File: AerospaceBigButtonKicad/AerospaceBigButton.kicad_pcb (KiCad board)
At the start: 2 copper layers, 120 x 80 mm, 20 parts, among them J1 Conn_01x07, J2 Conn_01x07, J3 Conn_01x02, J4 Conn_01x02, J5 Conn_01x02, Q1 Si7336ADP, SW1 BIGSWITCH, U1 AMS1117-5.0

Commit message: basic design done
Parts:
- removed R6: 100k, Resistor_SMD:R_0805_2012Metric
- removed R7: 27k, Resistor_SMD:R_0805_2012Metric
- added H1: MountingHole_Pad, MountingHole:MountingHole_3.2mm_M3_DIN965_Pad_TopBottom, F.Cu at (55.0, 20.0)
- added H2: MountingHole_Pad, MountingHole:MountingHole_3.2mm_M3_DIN965_Pad_TopBottom, F.Cu at (160.0, 20.0)
- added H3: MountingHole_Pad, MountingHole:MountingHole_3.2mm_M3_DIN965_Pad_TopBottom, F.Cu at (160.0, 90.0)
- added H4: MountingHole_Pad, MountingHole:MountingHole_3.2mm_M3_DIN965_Pad_TopBottom, F.Cu at (55.0, 90.0)
- added J6: Conn_01x03, Connector_JST:JST_PH_B3B-PH-K_1x03_P2.00mm_Vertical, F.Cu at (54.9, 56.4)
- moved R1 92.6 mm to (86.0, 77.7), turned to 90 degrees
- moved C1 89.0 mm to (81.2, 33.0)
- moved R4 86.3 mm to (85.8, 71.0)
- moved R5 85.0 mm to (85.8, 73.6), turned to 180 degrees
- moved R2 78.7 mm to (76.6, 57.6)
- moved R3 78.7 mm to (76.6, 59.8)
- moved R8 78.6 mm to (85.3, 58.2), turned to -90 degrees
- moved R9 75.1 mm to (81.8, 58.2), turned to -90 degrees
- moved C2 74.1 mm to (67.4, 54.8)
- moved U1 5.55 mm to (65.8, 48.6)
- moved J2 2.54 mm to (81.3, 63.5)
- moved SW1 2.46 mm to (125.0, 55.0)
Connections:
- J2 pad 3: /RGB -> /CONT
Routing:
- net Net-(Q1-G): track 0.00 -> 71.8 mm
- net +3V3: track 0.00 -> 52.5 mm
- net /BIGSWITCH: track 0.00 -> 50.5 mm
- net Net-(J4-Pin_1): track 0.00 -> 37.8 mm, vias 0 -> 2
- net /ARMED: track 0.00 -> 30.4 mm
- net VCC: track 0.00 -> 26.7 mm
- net +5V: track 0.00 -> 22.4 mm
- net /CONT: track 0.00 -> 13.1 mm
- net /VINSENSE: track 0.00 -> 9.63 mm
- net /FIRE: track 0.00 -> 6.23 mm
- net GND: vias 0 -> 32
- added copper zone on F.Cu, net /PYRO
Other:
- board size 120 x 80 mm -> 114.2 x 80.2 mm

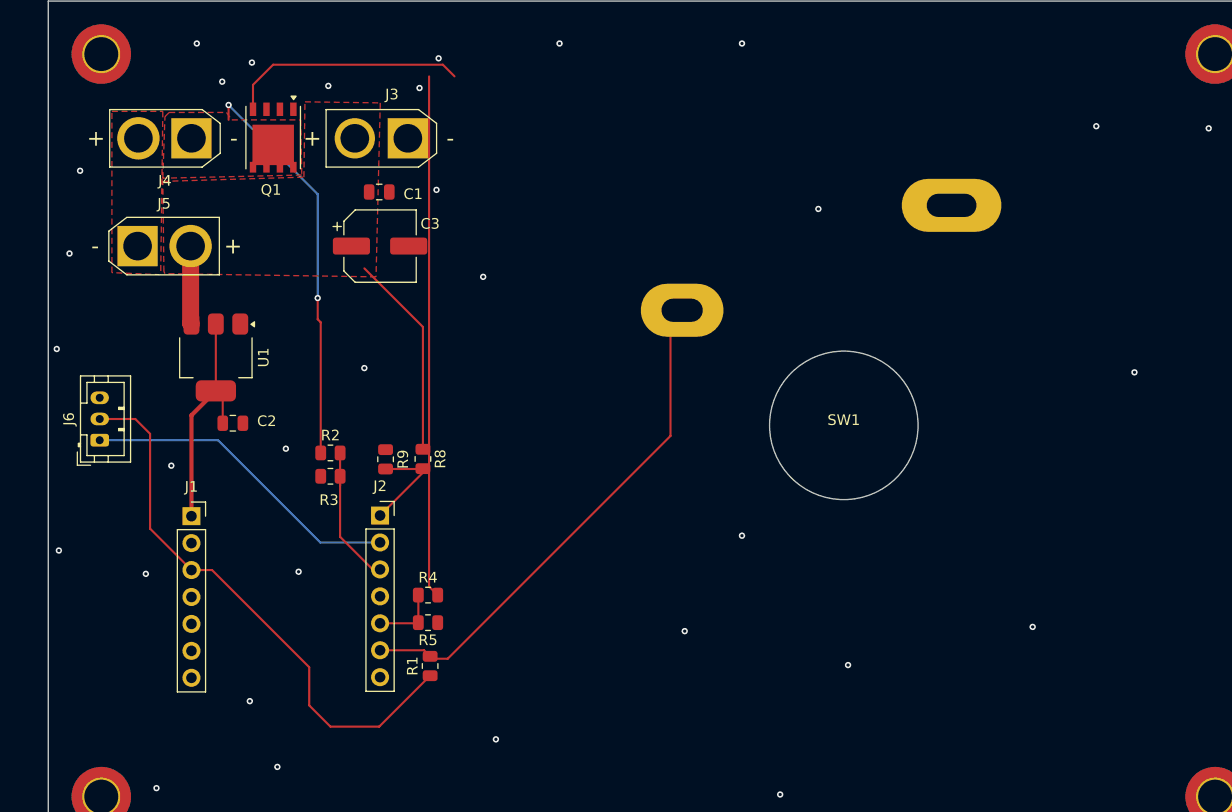
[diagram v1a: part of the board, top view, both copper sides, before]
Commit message: finalized design for now, added 5v driver for speaker
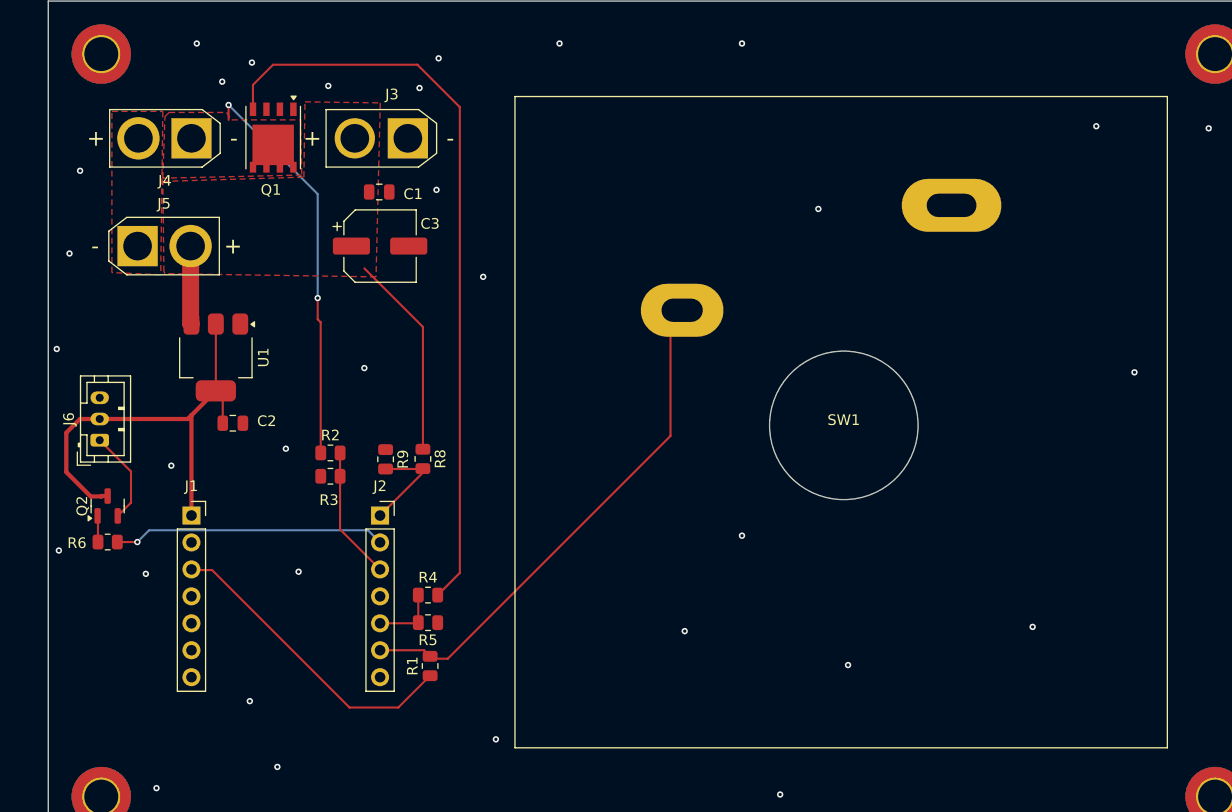
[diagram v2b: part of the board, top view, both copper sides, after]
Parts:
- added Q2: MMBT2222A, Package_TO_SOT_SMD:SOT-23, F.Cu at (55.6, 62.6)
- added R6: 1k, Resistor_SMD:R_0805_2012Metric, F.Cu at (55.6, 66.0)
- moved J1 0.06 mm to (63.5, 63.5)
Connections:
- J6 pad 1: /ARMED -> Net-(J6-Pin_1)
- J6 pad 2: +3V3 -> +5V
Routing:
- net +3V3: track 52.5 -> 29.1 mm
- net +5V: track 22.4 -> 43.4 mm
- net Net-(J6-Pin_1): track 0.00 -> 8.88 mm
- net /ARMED: track 30.4 -> 25.7 mm, vias 0 -> 1
- net Net-(Q2-B): track 0.00 -> 2.48 mm
- net Net-(Q1-G): track 71.8 -> 71.1 mm
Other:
- board text added: "R6"
